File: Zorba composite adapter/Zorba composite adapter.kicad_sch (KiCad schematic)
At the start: 17 parts, among them IC1 74LS00, IC3 74LS123, J1 Conn_02x04_Odd_Even, J2 RCA jack on rear panel, Q1 2N3904, U1 74LS175

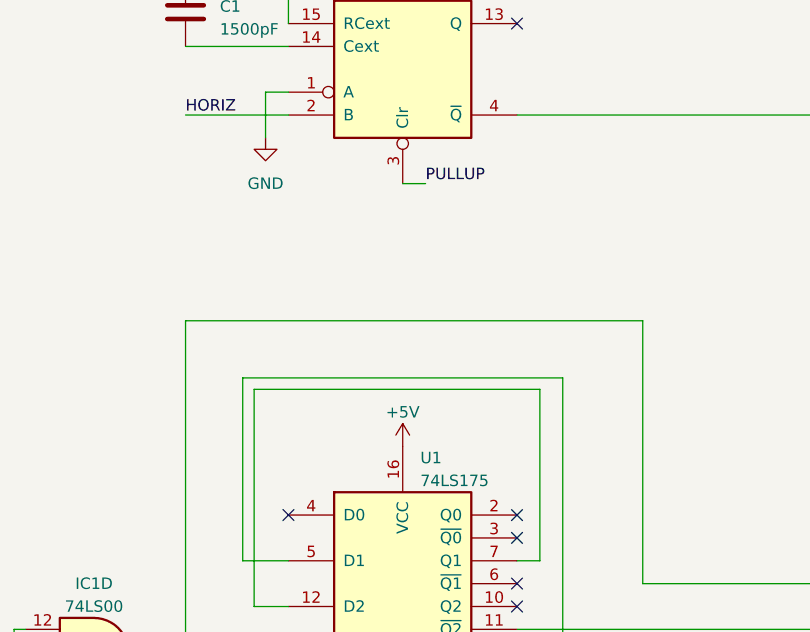
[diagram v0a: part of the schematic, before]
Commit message: Corrections to schematic
IC2 was mislabeled U1.

PULLUP connection to IC3 pin 3 was oriented toward the right, implying
that it's an output.
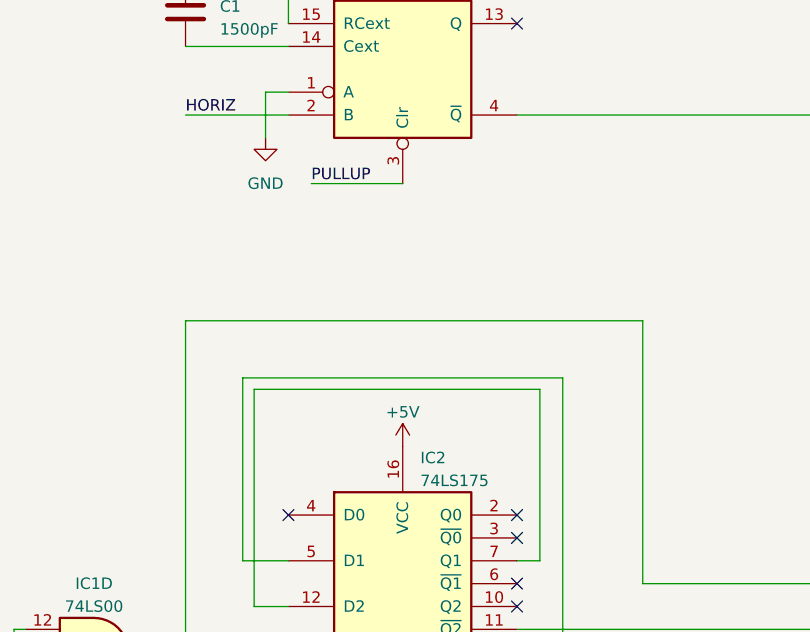
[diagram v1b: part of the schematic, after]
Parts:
- renumbered U1 to IC2
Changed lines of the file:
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@@
     (stroke (width 0) (type default))
   )
-  (wire (pts (xy 68.58 119.38) (xy 71.12 119.38))
+  (wire (pts (xy 68.58 119.38) (xy 58.42 119.38))
     (stroke (width 0) (type default))
   )
@@
     (effects (font (size 1.27 1.27)) (justify left bottom))
   )
-  (label "PULLUP" (at 71.12 119.38 0) (fields_autoplaced)
+  (label "PULLUP" (at 58.42 119.38 0) (fields_autoplaced)
     (effects (font (size 1.27 1.27)) (justify left bottom))
   )
@@
   (symbol (lib_id "74xx:74LS175") (at 68.58 166.37 0) (unit 1)
     (in_bom yes) (on_board yes) (dnp no) (fields_autoplaced)
-    (property "Reference" "U1" (at 70.5359 149.86 0)
+    (property "Reference" "IC2" (at 70.5359 149.86 0)
       (effects (font (size 1.27 1.27)) (justify left))
     )
@@
       (project "Zorba composite adapter"
         (path "/169d948f-f833-40a6-b230-21e2ec665763"
-          (reference "U1") (unit 1)
-        )
-      )
+          (reference "IC2") (unit 1)
+        )
+      )
